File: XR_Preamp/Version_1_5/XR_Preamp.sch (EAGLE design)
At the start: 19 parts, among them T1 2SC3324, T2 2SC3324

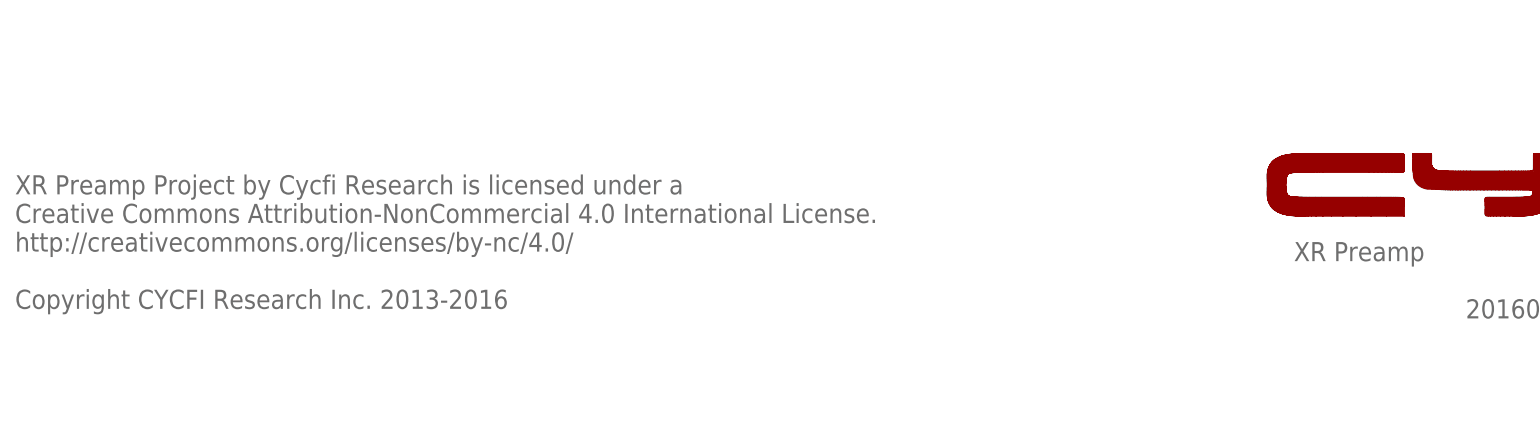
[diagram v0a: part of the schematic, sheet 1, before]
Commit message: Updated schematic licenses
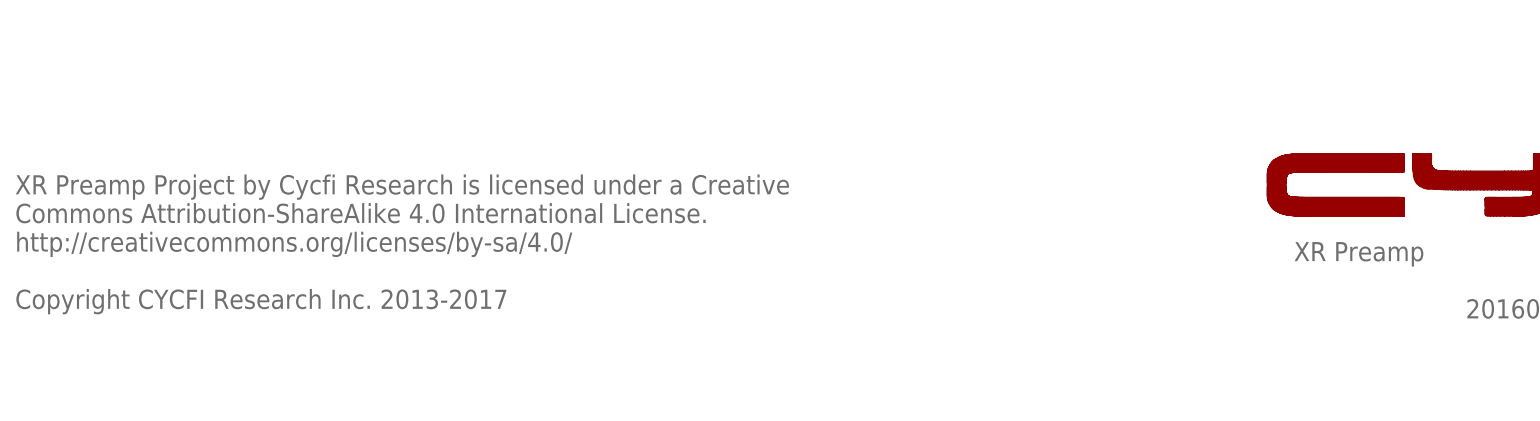
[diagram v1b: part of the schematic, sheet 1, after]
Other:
- note added: "XR Preamp Project by Cycfi Research is licensed under a Creative Commons Attribution-ShareAlike 4.0 International License. http://creativecommons.org/licenses/by-sa/4.0/ Copyright CYCFI Research Inc. 2013-2017"
- note removed: "XR Preamp Project by Cycfi Research is licensed under a Creative Commons Attribution-NonCommercial 4.0 International License. http://creativecommons.org/licenses/by-nc/4.0/ Copyright CYCFI Research Inc. 2013-2016"
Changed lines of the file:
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@@
 <text x="173.6725" y="98.7425" size="1.778" layer="95">NOTE:
 *Gain Adjustment Trimmer</text>
-<text x="177.8" y="19.05" size="2.54" layer="95">XR Preamp</text>
-<text x="252.73" y="6.985" size="2.1844" layer="95">v1.5</text>
-<text x="7.62" y="12.7" size="2.54" layer="95">XR Preamp Project by Cycfi Research is licensed under a
-Creative Commons Attribution-NonCommercial 4.0 International License.
-http://creativecommons.org/licenses/by-nc/4.0/
-Copyright CYCFI Research Inc. 2013-2016</text>
-<text x="200.66" y="11.43" size="2.54" layer="95">2016008</text>
+<text x="177.8" y="19.05" size="2.54" layer="95" font="vector">XR Preamp</text>
+<text x="252.73" y="6.985" size="2.1844" layer="95" font="vector">v1.5</text>
+<text x="7.62" y="12.7" size="2.54" layer="95" font="vector">XR Preamp Project by Cycfi Research is licensed under a Creative
+Commons Attribution-ShareAlike 4.0 International License.
+http://creativecommons.org/licenses/by-sa/4.0/
+Copyright CYCFI Research Inc. 2013-2017</text>
+<text x="200.66" y="11.43" size="2.54" layer="95" font="vector">2016008</text>
 <wire x1="192.47528125" y1="25.047221875" x2="190.115640625" y2="25.047221875" width="0" layer="94"/>
 <wire x1="190.115640625" y1="25.047221875" x2="188.10833125" y2="25.047225" width="0" layer="94"/>
@@
 <wire x1="235.1615625" y1="25.047221875" x2="232.684540625" y2="25.047221875" width="0" layer="94"/>
 <wire x1="232.684540625" y1="25.047221875" x2="232.684540625" y2="33.356103125" width="0" layer="94"/>
-<polygon width="0" layer="94">
+<polygon width="0.1524" layer="94">
 <vertex x="192.47528125" y="25.047221875"/>
 <vertex x="178.450640625" y="25.047221875"/>
@@
 <vertex x="232.684540625" y="25.047221875"/>
 </polygon>
-<text x="248.92" y="1.27" size="2.54" layer="94">1/2</text>
+<text x="248.92" y="1.27" size="2.54" layer="94" font="vector">1/2</text>
 </plain>
 <instances>
@@
 <text x="128.27" y="85.4075" size="1.778" layer="95">VCC</text>
 <text x="101.6" y="137.16" size="5.08" layer="95">CASTELLATED PADS</text>
-<text x="177.8" y="19.05" size="2.54" layer="95">XR Preamp</text>
-<text x="252.73" y="6.985" size="2.1844" layer="95">v1.5</text>
-<text x="7.62" y="12.7" size="2.54" layer="95">XR Preamp Project by Cycfi Research is licensed under a
-Creative Commons Attribution-NonCommercial 4.0 International License.
-http://creativecommons.org/licenses/by-nc/4.0/
-Copyright CYCFI Research Inc. 2013-2016</text>
-<text x="200.66" y="11.43" size="2.54" layer="95">2016008</text>
+<text x="177.8" y="19.05" size="2.54" layer="95" font="fixed">XR Preamp</text>
+<text x="252.73" y="6.985" size="2.1844" layer="95" font="fixed">v1.5</text>
+<text x="7.62" y="12.7" size="2.54" layer="95" font="fixed">XR Preamp Project by Cycfi Research is licensed under a Creative
+Commons Attribution-ShareAlike 4.0 International License.
+http://creativecommons.org/licenses/by-sa/4.0/
+Copyright CYCFI Research Inc. 2013-2017</text>
+<text x="200.66" y="11.43" size="2.54" layer="95" font="fixed">2016008</text>
 <wire x1="192.47528125" y1="25.047221875" x2="190.115640625" y2="25.047221875" width="0" layer="94"/>
 <wire x1="190.115640625" y1="25.047221875" x2="188.10833125" y2="25.047225" width="0" layer="94"/>
@@
 <vertex x="232.684540625" y="25.047221875"/>
 </polygon>
-<text x="248.92" y="1.27" size="2.54" layer="94">2/2</text>
+<text x="248.92" y="1.27" size="2.54" layer="94" font="fixed">2/2</text>
 </plain>
 <instances>
@@
 <instance part="FRAME3" gate="G$1" x="0" y="0"/>
 <instance part="FRAME3" gate="G$2" x="162.56" y="0" smashed="yes">
-<attribute name="LAST_DATE_TIME" x="175.26" y="1.27" size="2.54" layer="94" font="vector"/>
+<attribute name="LAST_DATE_TIME" x="175.26" y="1.27" size="2.54" layer="94" font="fixed"/>
 </instance>
 </instances>
